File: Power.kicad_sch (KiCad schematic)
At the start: 44 parts, among them IC1 TPS25730DREFR, J1 Conn_01x02_Pin, J2 USB_C_Receptacle_USB2.0_16P, U2 TVS1800DRV, U3 INA180A1

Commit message: 3/8/2025
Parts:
- removed C2: 4.7 uF, symbol Device:C
- removed C8: 10 uF, symbol Device:C
- removed C9: 1 uF, symbol Device:C
- added C12: 4.7 uF, Capacitor_SMD:C_0805_2012Metric, symbol Device:C
- added C73, C74, C75, C76: 10 nF, Capacitor_SMD:C_0603_1608Metric, symbol Device:C
- added R49: 10k, Resistor_SMD:R_0603_1608Metric, symbol Device:R_US
- C10: renamed from C6; footprint (none) -> Capacitor_SMD:C_1210_3225Metric
- C11: renamed from C5; footprint (none) -> Capacitor_SMD:C_1210_3225Metric
- C13: renamed from C10; footprint (none) -> Capacitor_SMD:C_0805_2012Metric
- C14: renamed from C3; footprint (none) -> Capacitor_SMD:C_0603_1608Metric
- C16: renamed from C4; footprint (none) -> Capacitor_SMD:C_0603_1608Metric
- C6: renamed from C11; value 0.1 uF -> 100 nF; footprint (none) -> Capacitor_SMD:C_0603_1608Metric
- C7: footprint (none) -> Capacitor_SMD:C_1210_3225Metric
- C8: renamed from C1; value 10 uF -> 4.7 uF; footprint (none) -> Capacitor_SMD:C_0805_2012Metric
- C9: renamed from C12; footprint (none) -> Capacitor_SMD:C_0805_2012Metric
- D3, D4, D5, D6: footprint (none) -> Diode_SMD:D_0603_1608Metric
- J4: renamed from J1; footprint (none) -> Connector_PinHeader_2.54mm:PinHeader_1x02_P2.54mm_Vertical
- R10: renamed from R8; value 5.1k -> 100k; footprint (none) -> Resistor_SMD:R_0603_1608Metric
- R11: renamed from R12; value R_US -> 5.1k; footprint (none) -> Resistor_SMD:R_0603_1608Metric
- R12: renamed from R13; value R_US -> 1k; footprint (none) -> Resistor_SMD:R_0603_1608Metric
- R13: renamed from R3; footprint (none) -> Resistor_SMD:R_0603_1608Metric
- R14: renamed from R10; value 5.1k -> 100k; footprint (none) -> Resistor_SMD:R_0603_1608Metric
- R15: renamed from R14; value R_US -> 23.2k; footprint (none) -> Resistor_SMD:R_0603_1608Metric
- R16: renamed from R15; value R_US -> 5.1k; footprint (none) -> Resistor_SMD:R_0603_1608Metric
- R17: renamed from R?; footprint (none) -> Resistor_SMD:R_0603_1608Metric
- R18: renamed from R16; footprint (none) -> Resistor_SMD:R_0603_1608Metric
- R19: renamed from R17; footprint (none) -> Resistor_SMD:R_0603_1608Metric
- R20: renamed from R18; footprint (none) -> Resistor_SMD:R_0603_1608Metric
- R21: renamed from R19; footprint (none) -> Resistor_SMD:R_0603_1608Metric
- R3: renamed from R4; value 5.1k -> 100k; footprint (none) -> Resistor_SMD:R_0603_1608Metric
- R4: renamed from R1; value 0.025 -> 0.025R; footprint (none) -> Capacitor_SMD:C_1206_3216Metric
- R5: renamed from R6; value 5.1k -> 100k; footprint (none) -> Resistor_SMD:R_0603_1608Metric
- R6: renamed from R7; value R_US -> 1k; footprint (none) -> Resistor_SMD:R_0603_1608Metric
- R7: renamed from R9; value R_US -> 5.1k; footprint (none) -> Resistor_SMD:R_0603_1608Metric
- R8: renamed from R5; value R_US -> 5.1k; footprint (none) -> Resistor_SMD:R_0603_1608Metric
- R9: renamed from R11; value R_US -> 23.2k; footprint (none) -> Resistor_SMD:R_0603_1608Metric
- renumbered J2 to J3
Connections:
- net VBUS_TO_LDO is gone; now on net VBUS_RAW-2: IC1.32 (VBUS_1), IC1.33 (VBUS_2), IC1.43 (VBUS_3)
- net ADCIN1: now also S1.15, S1.16; no longer S1.10, S1.9
- net ADCIN1-A: now also S1.2; no longer S1.8
- net ADCIN1-B: now also S1.1; no longer S1.7
- net ADCIN2: now also S1.13, S1.14; no longer S1.11, S1.12
- net ADCIN2-A: now also S1.4; no longer S1.6
- net ADCIN2-B: now also S1.3; no longer S1.5
- net ADCIN3: now also S1.11, S1.12; no longer S1.13, S1.14
- net ADCIN3-A: now also S1.6; no longer S1.4
- net ADCIN3-B: now also S1.5; no longer S1.3
- net ADCIN4: now also S1.10, S1.9; no longer S1.15, S1.16
- net ADCIN4-A: now also S1.8; no longer S1.1, S1.2
- net ADCIN4-B: now also S1.7
- net GND: now also C12.2, C73.2, C74.2, C75.2, C76.2
- net LDO_3V3: now also R13.1, R49.1; no longer R18.1, R19.1, R20.1, R21.1
- net VBUS_RAW-2: now also C12.1, C73.1, C74.1, C75.1, C76.1
- net +3.3V renamed +3V3
- net +3V3: now also R18.1, R19.1, R20.1, R21.1; no longer IC1.18 (~{FAULT_IN}), R13.1
- new net ~{FAULT_IN}: IC1.18 (~{FAULT_IN}), R49.2
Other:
- note added: "Jumper included to GND to enforce dead battery mode or route power from 3.3V rail"
- note removed: "25V Voltage rating"
- note removed: "Jumper included to enforce dead battery mode if not placed"
- moved on the sheet: C6, C8, C9, J3, R4, U2, U3

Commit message: Layout draft complete
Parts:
- removed J4: Conn_01x02_Pin, Connector_PinHeader_2.54mm:PinHeader_1x02_P2.54mm_Vertical, symbol Connector:Conn_01x02_Pin
- added TP1, TP2: TestPoint, TestPoint:TestPoint_Pad_D1.0mm, symbol Connector:TestPoint
- renumbered IC1 to U13
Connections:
- net GND: now also J3.S1 (SHIELD)
- net VBUS_SENSE: now also TP2.1
- net 3V3-RTC: no longer names the net of B1.1
- net 3V3-RTC: no longer B1.3
- net VBUS_RAW-1 renamed VBUS_RAW_1
- net VBUS_RAW_1: now also TP1.1
- net VBUS_RAW-2 renamed VBUS_RAW_2
- new net 3V_RTC: B1.3
- no-connect marks 0 -> 3
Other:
- note added: "Status LEDs"
- note removed: "VIN_3V3 is input"
- title: (none) -> Jakka1
- moved on the sheet: B1, C13, D1, D2, D3, D4, D5, D6, R10, R11, R12, R14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

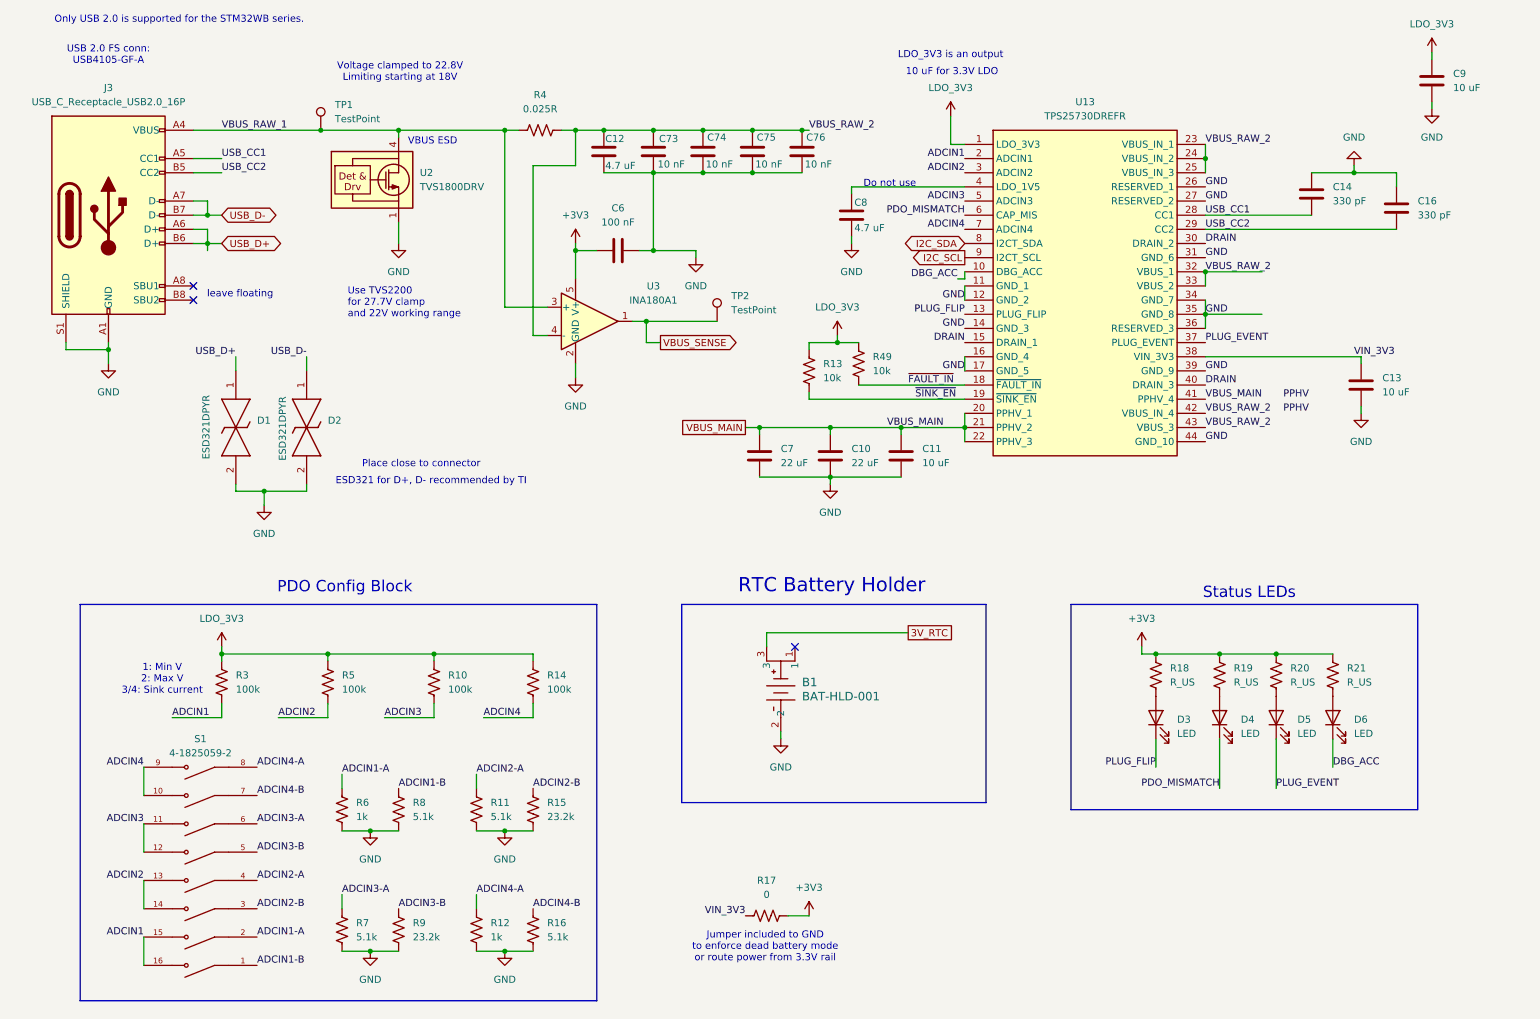
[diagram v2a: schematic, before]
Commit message: First draft of design output, schematic, and layout complete
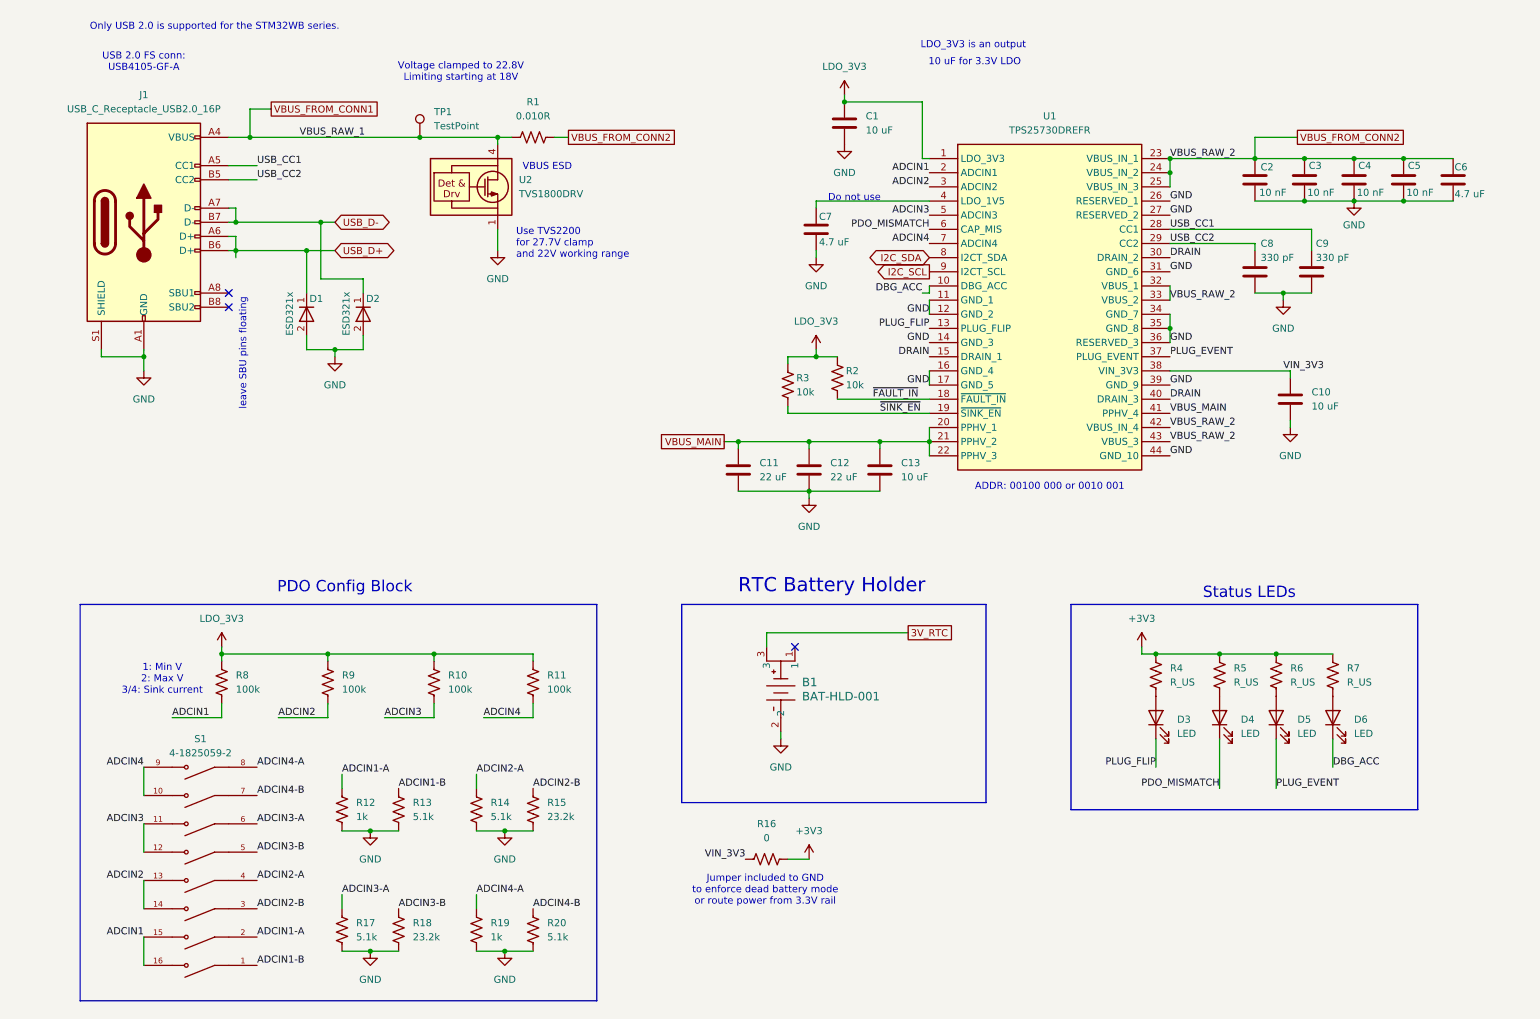
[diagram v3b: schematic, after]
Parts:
- removed C6: 100 nF, Capacitor_SMD:C_0603_1608Metric, symbol Device:C
- removed D1, D2: ESD321DPYR, jka_library:DPY_R-PX1SON-N2_, symbol jka_library:ESD321DPYR
- removed R4: 0.025R, Capacitor_SMD:C_1206_3216Metric, symbol Device:R_US
- removed TP2: TestPoint, TestPoint:TestPoint_Pad_D1.0mm, symbol Connector:TestPoint
- removed U3: INA180A1, Package_TO_SOT_SMD:SOT-23-5, symbol Amplifier_Current:INA180A1
- added D1, D2: ESD321x, jka_library:SODFL1608X77N, symbol jka_library:ESD321DYAR
- added R1: 0.010R, Capacitor_SMD:C_1206_3216Metric, symbol Device:R_US
- renumbered C9 to C1, C13 to C10, C7 to C11, C10 to C12, C11 to C13, C73 to C2, C74 to C3, C75 to C4, C76 to C5, C12 to C6, C8 to C7, C16 to C8, C14 to C9, J3 to J1, R14 to R11, R6 to R12, R8 to R13, R11 to R14, R17 to R16, R7 to R17, R9 to R18, R12 to R19, R49 to R2, R16 to R20, R13 to R3, R18 to R4, R19 to R5, R20 to R6, R21 to R7, R3 to R8, R5 to R9, U13 to U1
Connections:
- net GND: now also C8.2, C9.2, D1.2 (A), D2.2 (A); no longer C8.1, C9.1
- net USB_CC1: now also C9.1; no longer C9.2
- net USB_CC2: now also C8.1; no longer C8.2
- net USB_D+: now also D1.1 (K)
- net USB_D-: now also D2.1 (K)
- net VBUS_RAW_1 renamed VBUS_FROM_CONN1
- net VBUS_FROM_CONN1: now also R1.2
- net VBUS_RAW_2 renamed VBUS_FROM_CONN2
- net VBUS_FROM_CONN2: now also R1.1
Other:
- note added: "ADDR: 00100 000 or 0010 001"
- note added: "leave SBU pins floating"
- note removed: "ESD321 for D+, D- recommended by TI"
- note removed: "Place close to connector"
- note removed: "leave floating"
- company: (none) -> Jacob Kapala
- moved on the sheet: C1, C10, C11, C12, C13, C2, C3, C4, C5, C6, C7, C8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
